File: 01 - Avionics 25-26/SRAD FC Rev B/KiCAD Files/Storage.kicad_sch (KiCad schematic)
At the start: 0 parts

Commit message: Import storage footprint
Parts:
- added U1: W25Q128JVSIQ, W25Q128JVSIQ:SOIC127P790X216-8N, symbol W25Q128JVSIQ:W25Q128JVSIQ
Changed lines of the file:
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@@
 	(generator_version "9.0")
 	(paper "A4")
+	(symbol
+		(lib_id "W25Q128JVSIQ:W25Q128JVSIQ")
+		(at 144.78 90.17 0)
+		(unit 1)
+		(exclude_from_sim no)
+		(in_bom yes)
+		(on_board yes)
+		(dnp no)
+		(fields_autoplaced yes)
+		(property "Reference" "U1"
+			(at 144.78 69.85 0)
+			(effects
+				(font
+					(size 1.27 1.27)
+				)
+			)
+		)
+		(property "Value" "W25Q128JVSIQ"
+			(at 144.78 72.39 0)
+			(effects
+				(font
+					(size 1.27 1.27)
+				)
+			)
+		)
+		(property "Footprint" "W25Q128JVSIQ:SOIC127P790X216-8N"
+			(at 144.78 90.17 0)
+			(effects
+				(font
+					(size 1.27 1.27)
+				)
+				(justify bottom)
+				(hide yes)
+			)
+		)
+		(property "Datasheet" ""
+			(at 144.78 90.17 0)
+			(effects
+				(font
+					(size 1.27 1.27)
+				)
+				(hide yes)
+			)
+		)
+		(property "Description" ""
+			(at 144.78 90.17 0)
+			(effects
+				(font
+					(size 1.27 1.27)
+				)
+				(hide yes)
+			)
+		)
+		(property "PARTREV" "I"
+			(at 144.78 90.17 0)
+			(effects
+				(font
+					(size 1.27 1.27)
+				)
+				(justify bottom)
+				(hide yes)
+			)
+		)
+		(property "STANDARD" "IPC-7351B"
+			(at 144.78 90.17 0)
+			(effects
+				(font
+					(size 1.27 1.27)
+				)
+				(justify bottom)
+				(hide yes)
+			)
+		)
+		(property "MAXIMUM_PACKAGE_HEIGHT" "2.16 mm"
+			(at 144.78 90.17 0)
+			(effects
+				(font
+					(size 1.27 1.27)
+				)
+				(justify bottom)
+				(hide yes)
+			)
+		)
+		(property "MANUFACTURER" "Winbond Electronics"
+			(at 144.78 90.17 0)
+			(effects
+				(font
+					(size 1.27 1.27)
+				)
+				(justify bottom)
+				(hide yes)
+			)
+		)
+		(pin "1"
+		)
+		(pin "6"
+		)
+		(pin "4"
+		)
+		(pin "7"
+		)
+		(pin "5"
+		)
+		(pin "2"
+		)
+		(pin "3"
+		)
+		(pin "8"
+		)
+		(instances
+			(project ""
+				(path "/1dd9e63a-24f2-43c6-ae21-66b89e6998f2/7a96f78f-7769-410f-82f2-b37baf0f0866"
+					(reference "U1")
+					(unit 1)
+				)
+			)
+		)
+	)
 )

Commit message: Info to Storage and RF Module
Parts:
- Storage: renamed from U1; Link (none) -> https://www.digikey.com/en/products/detail/winbond-electron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
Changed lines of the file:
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@@
 		(dnp no)
 		(fields_autoplaced yes)
-		(property "Reference" "U1"
+		(property "Reference" "Storage"
 			(at 144.78 69.85 0)
 			(effects
@@
 			)
 		)
-		(property "Datasheet" ""
+		(property "Datasheet" "https://mm.digikey.com/Volume0/opasdata/d220001/medias/docus/7161/256_W25Q128JV.pdf"
 			(at 144.78 90.17 0)
 			(effects
@@
 			)
 		)
-		(property "Description" ""
+		(property "Description" "3V 128M-BIT  SERIAL FLASH MEMORY WITH   DUAL/QUAD SPI"
+			(at 144.78 90.17 0)
+			(effects
+				(font
+					(size 1.27 1.27)
+				)
+				(hide yes)
+			)
+		)
+		(property "Link" "https://www.digikey.com/en/products/detail/winbond-electronics/W25Q128JVSIQ/5803943"
 			(at 144.78 90.17 0)
 			(effects
@@
 			(project ""
 				(path "/1dd9e63a-24f2-43c6-ae21-66b89e6998f2/7a96f78f-7769-410f-82f2-b37baf0f0866"
-					(reference "U1")
+					(reference "Storage")
 					(unit 1)
 				)

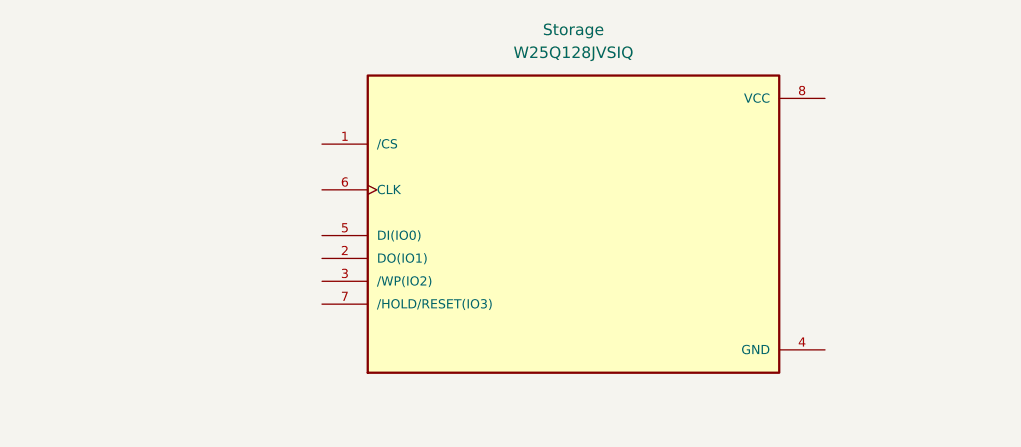
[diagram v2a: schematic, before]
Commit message: Added Storage and RF Module Circuits with Labels for Future Connects
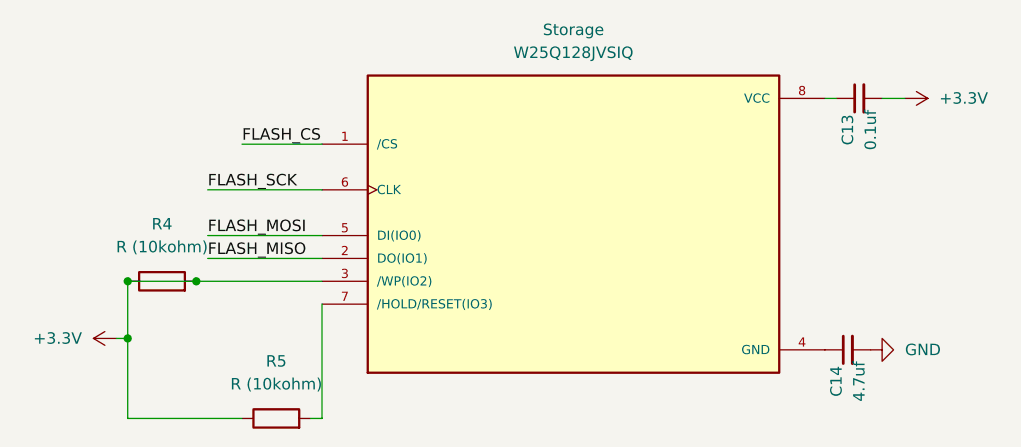
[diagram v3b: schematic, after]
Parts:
- added C13: 0.1uf, symbol Device:C_Small
- added C14: 4.7uf, symbol Device:C_Small
- added R4, R5: R (10kohm), symbol Device:R
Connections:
- net FLASH_CS: now reaches Storage.1 (/CS)
- net FLASH_MISO: now reaches Storage.2 (DO(IO1))
- net +3.3V: now reaches Storage.3 (/WP(IO2))
- net +3.3V: now also C13.2, R4.1, R4.2, R5.1
- net at Storage.4 (GND): now also C14.1
- net FLASH_MOSI: now reaches Storage.5 (DI(IO0))
- net FLASH_SCK: now reaches Storage.6 (CLK)
- net at Storage.7 (/HOLD/RESET(IO3)): now also R5.2
- net at Storage.8 (VCC): now also C13.1
- new net GND: C14.2

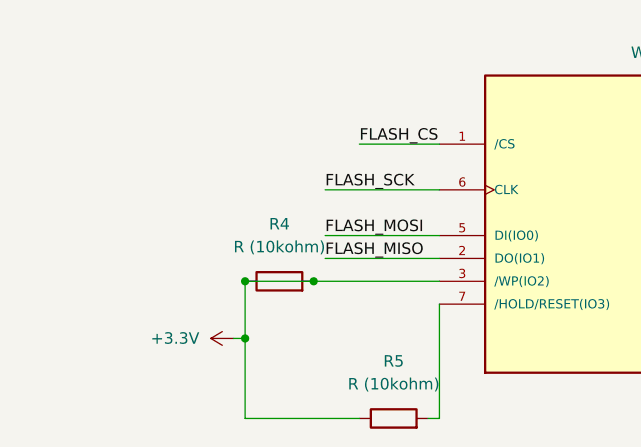
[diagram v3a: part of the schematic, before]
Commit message: Updated Sheet Pins
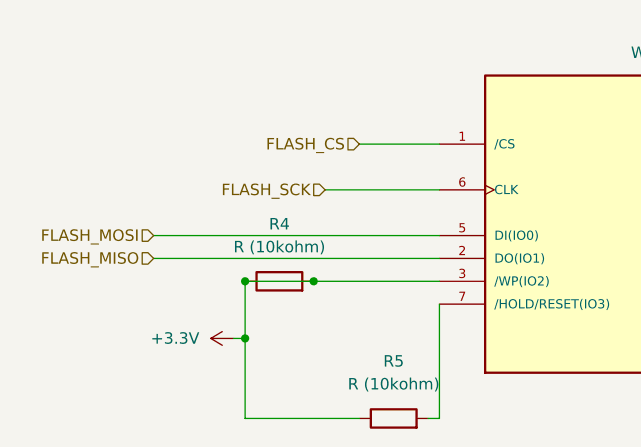
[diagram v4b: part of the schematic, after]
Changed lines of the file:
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@@
-	(wire
-		(pts
-			(xy 104.14 95.25) (xy 116.84 95.25)
-		)
-		(stroke
-			(width 0)
-			(type default)
-		)
-	)
 	(wire
 		(pts
@@
 	(wire
 		(pts
-			(xy 104.14 92.71) (xy 116.84 92.71)
+			(xy 85.09 92.71) (xy 116.84 92.71)
 		)
 		(stroke
@@
 	(wire
 		(pts
+			(xy 85.09 95.25) (xy 116.84 95.25)
+		)
+		(stroke
+			(width 0)
+			(type default)
+		)
+	)
+	(wire
+		(pts
 			(xy 93.98 104.14) (xy 95.25 104.14)
 		)
@@
 		)
 	)
-	(label "FLASH_SCK"
-		(at 104.14 87.63 0)
+	(hierarchical_label "FLASH_SCK"
+		(shape input)
+		(at 104.14 87.63 180)
 		(effects
 			(font
 				(size 1.27 1.27)
 			)
-			(justify left bottom)
+			(justify right)
 		)
 	)
-	(label "FLASH_CS"
-		(at 107.95 82.55 0)
+	(hierarchical_label "FLASH_MOSI"
+		(shape input)
+		(at 85.09 92.71 180)
 		(effects
 			(font
 				(size 1.27 1.27)
 			)
-			(justify left bottom)
+			(justify right)
 		)
 	)
-	(label "FLASH_MISO"
-		(at 104.14 95.25 0)
+	(hierarchical_label "FLASH_MISO"
+		(shape input)
+		(at 85.09 95.25 180)
 		(effects
 			(font
 				(size 1.27 1.27)
 			)
-			(justify left bottom)
+			(justify right)
 		)
 	)
-	(label "FLASH_MOSI"
-		(at 104.14 92.71 0)
+	(hierarchical_label "FLASH_CS"
+		(shape input)
+		(at 107.95 82.55 180)
 		(effects
 			(font
 				(size 1.27 1.27)
 			)
-			(justify left bottom)
+			(justify right)
 		)
 	)

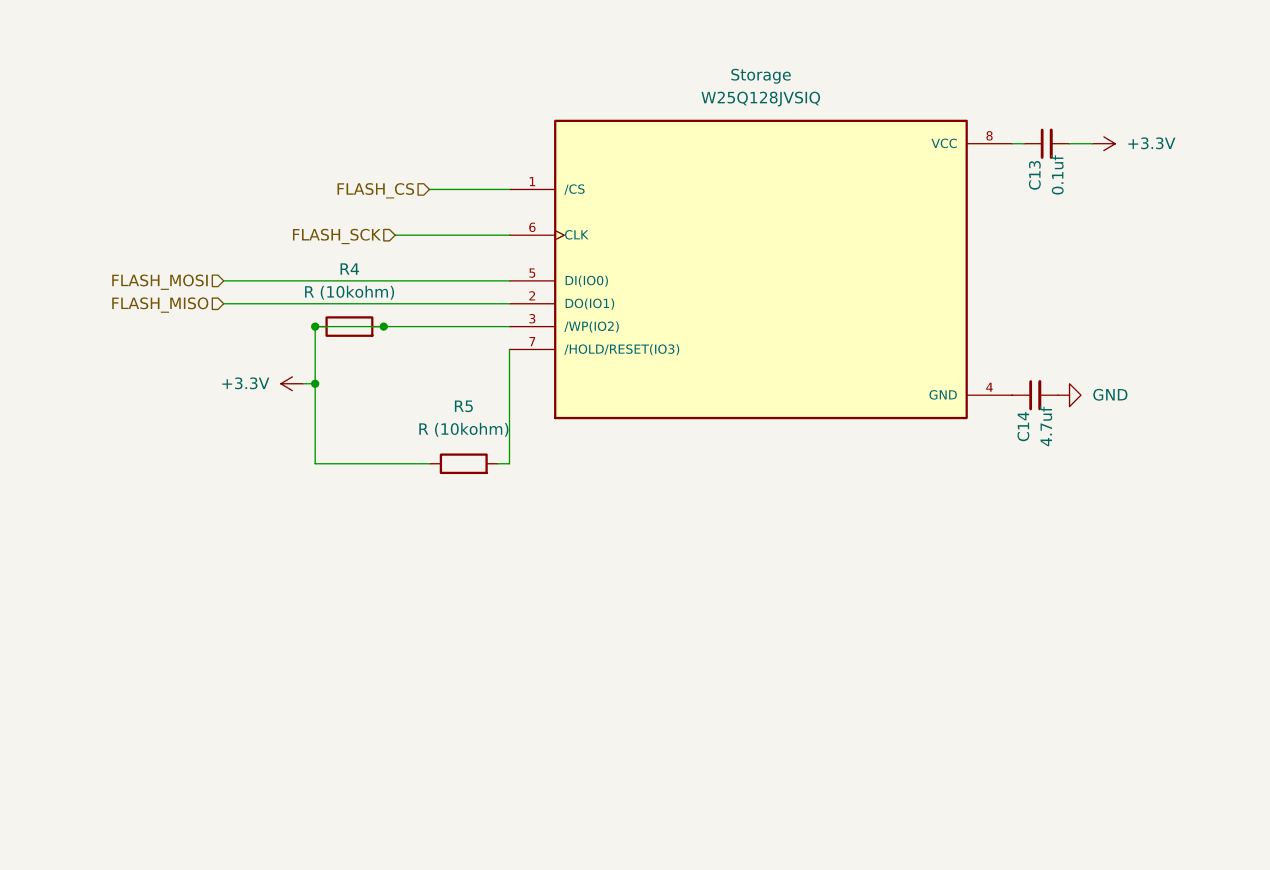
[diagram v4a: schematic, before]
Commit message: added power as hierarchical sheet pins
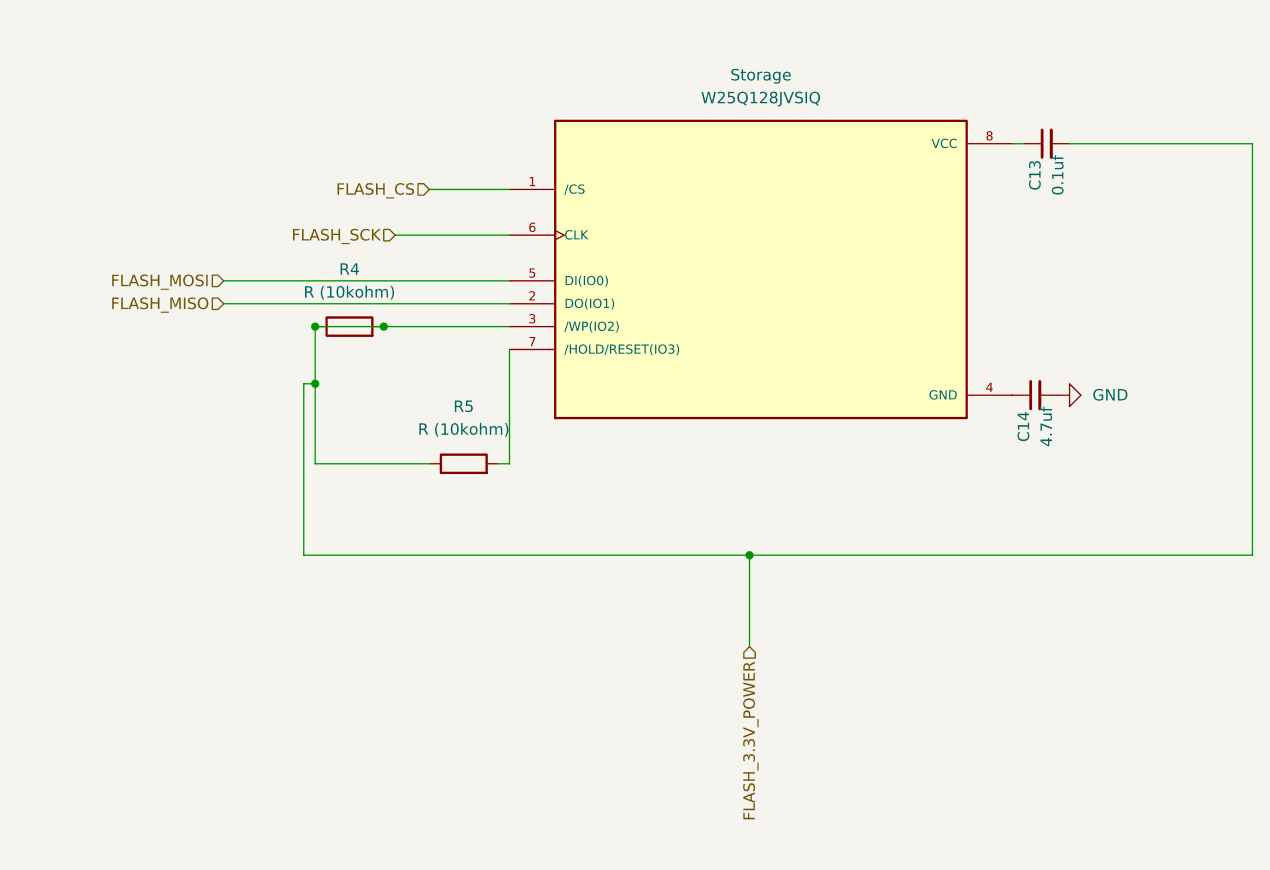
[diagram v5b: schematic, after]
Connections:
- net +3.3V renamed FLASH_3.3V_POWER
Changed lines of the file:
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@@
+	)
+	(junction
+		(at 143.51 123.19)
+		(diameter 0)
+		(color 0 0 0 0)
 	)
 	(junction
@@
 	(wire
 		(pts
+			(xy 199.39 123.19) (xy 143.51 123.19)
+		)
+		(stroke
+			(width 0)
+			(type default)
+		)
+	)
+	(wire
+		(pts
 			(xy 104.14 87.63) (xy 116.84 87.63)
 		)
@@
 	(wire
 		(pts
-			(xy 179.07 77.47) (xy 181.61 77.47)
+			(xy 93.98 104.14) (xy 93.98 123.19)
+		)
+		(stroke
+			(width 0)
+			(type default)
+		)
+	)
+	(wire
+		(pts
+			(xy 179.07 77.47) (xy 199.39 77.47)
 		)
 		(stroke
@@
 	(wire
 		(pts
+			(xy 199.39 77.47) (xy 199.39 123.19)
+		)
+		(stroke
+			(width 0)
+			(type default)
+		)
+	)
+	(wire
+		(pts
+			(xy 93.98 123.19) (xy 143.51 123.19)
+		)
+		(stroke
+			(width 0)
+			(type default)
+		)
+	)
+	(wire
+		(pts
+			(xy 143.51 123.19) (xy 143.51 133.35)
+		)
+		(stroke
+			(width 0)
+			(type default)
+		)
+	)
+	(wire
+		(pts
 			(xy 93.98 104.14) (xy 95.25 104.14)
 		)
@@
 		)
 	)
+	(hierarchical_label "FLASH_3.3V_POWER"
+		(shape input)
+		(at 143.51 133.35 270)
+		(effects
+			(font
+				(size 1.27 1.27)
+			)
+			(justify right)
+		)
+	)
 	(hierarchical_label "FLASH_CS"
 		(shape input)
@@
 			)
 			(justify right)
-		)
-	)
-	(symbol
-		(lib_id "power:+3.3V")
-		(at 93.98 104.14 90)
-		(unit 1)
-		(exclude_from_sim no)
-		(in_bom yes)
-		(on_board yes)
-		(dnp no)
-		(fields_autoplaced yes)
-		(property "Reference" "#PWR021"
-			(at 97.79 104.14 0)
-			(effects
-				(font
-					(size 1.27 1.27)
-				)
-				(hide yes)
-			)
-		)
-		(property "Value" "+3.3V"
-			(at 90.17 104.1399 90)
-			(effects
-				(font
-					(size 1.27 1.27)
-				)
-				(justify left)
-			)
-		)
-		(property "Footprint" ""
-			(at 93.98 104.14 0)
-			(effects
-				(font
-					(size 1.27 1.27)
-				)
-				(hide yes)
-			)
-		)
-		(property "Datasheet" ""
-			(at 93.98 104.14 0)
-			(effects
-				(font
-					(size 1.27 1.27)
-				)
-				(hide yes)
-			)
-		)
-		(property "Description" "Power symbol creates a global label with name \"+3.3V\""
-			(at 93.98 104.14 0)
-			(effects
-				(font
-					(size 1.27 1.27)
-				)
-				(hide yes)
-			)
-		)
-		(pin "1"
-		)
-		(instances
-			(project "SRAD FC Rev B"
-				(path "/1dd9e63a-24f2-43c6-ae21-66b89e6998f2/7a96f78f-7769-410f-82f2-b37baf0f0866"
-					(reference "#PWR021")
-					(unit 1)
-				)
-			)
 		)
 	)
@@
 					(unit 1)
 				)
-			)
-		)
-	)
-	(symbol
-		(lib_id "power:+3.3V")
-		(at 181.61 77.47 270)
-		(unit 1)
-		(exclude_from_sim no)
-		(in_bom yes)
-		(on_board yes)
-		(dnp no)
-		(fields_autoplaced yes)
-		(property "Reference" "#PWR019"
-			(at 177.8 77.47 0)
-			(effects
-				(font
-					(size 1.27 1.27)
-				)
-				(hide yes)
-			)
-		)
-		(property "Value" "+3.3V"
-			(at 185.42 77.4699 90)
-			(effects
-				(font
-					(size 1.27 1.27)
-				)
-				(justify left)
-			)
-		)
-		(property "Footprint" ""
-			(at 181.61 77.47 0)
-			(effects
-				(font
-					(size 1.27 1.27)
-				)
-				(hide yes)
-			)
-		)
-		(property "Datasheet" ""
-			(at 181.61 77.47 0)
-			(effects
-				(font
-					(size 1.27 1.27)
-				)
-				(hide yes)
-			)
-		)
-		(property "Description" "Power symbol creates a global label with name \"+3.3V\""
-			(at 181.61 77.47 0)
-			(effects
-				(font
-					(size 1.27 1.27)
-				)
-				(hide yes)
-			)
-		)
-		(pin "1"
-		)
-		(instances
-			(project "SRAD FC Rev B"
-				(path "/1dd9e63a-24f2-43c6-ae21-66b89e6998f2/7a96f78f-7769-410f-82f2-b37baf0f0866"
-					(reference "#PWR019")
-					(unit 1)
-				)

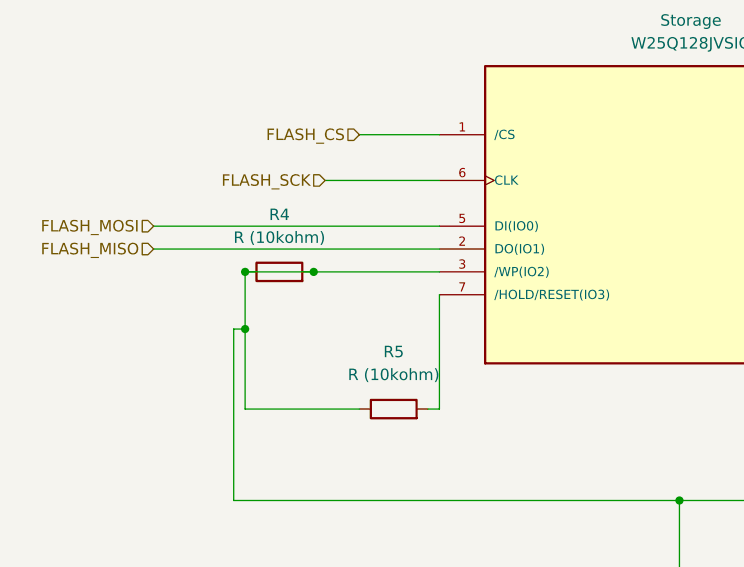
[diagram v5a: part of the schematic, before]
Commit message: general fixes for sheet sheet, ERC error fixes
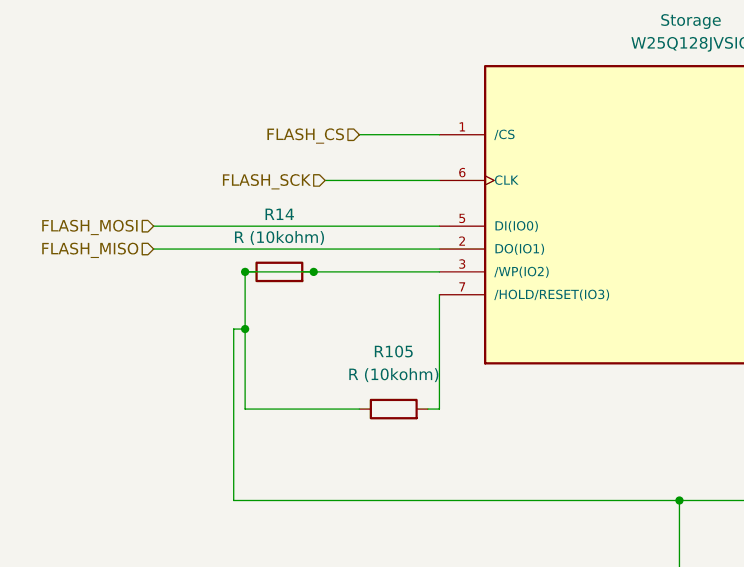
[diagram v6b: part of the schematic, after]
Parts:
- renumbered R5 to R105, R4 to R14
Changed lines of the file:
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@@
 		(dnp no)
 		(fields_autoplaced yes)
-		(property "Reference" "R5"
+		(property "Reference" "R105"
 			(at 111.76 106.68 90)
 			(effects
@@
 			(project "SRAD FC Rev B"
 				(path "/1dd9e63a-24f2-43c6-ae21-66b89e6998f2/7a96f78f-7769-410f-82f2-b37baf0f0866"
-					(reference "R5")
+					(reference "R105")
 					(unit 1)
 				)
@@
 		(dnp no)
 		(fields_autoplaced yes)
-		(property "Reference" "R4"
+		(property "Reference" "R14"
 			(at 99.06 91.44 90)
 			(effects
@@
 			(project "SRAD FC Rev B"
 				(path "/1dd9e63a-24f2-43c6-ae21-66b89e6998f2/7a96f78f-7769-410f-82f2-b37baf0f0866"
-					(reference "R4")
+					(reference "R14")
 					(unit 1)
 				)
